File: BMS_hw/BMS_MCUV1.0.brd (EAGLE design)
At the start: 60 x 30 mm, 48 parts, among them IC2 SST25VF020B804ISA, J1 22-27-2051-05, J2 22-27-2051-05, J3 22-27-2041-04, J4 22-27-2051-05, Q2 32.768kHz, U1 NCP1117LP-PG, X1 87758-2016

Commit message: baord sdsahdj
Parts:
- moved R7 50.7 mm to (52.2, 24.6), turned to 270 degrees
- moved U1 49.0 mm to (6.99, 19.1), turned to 90 degrees
- moved C4 38.8 mm to (13.2, 21.6), turned to 270 degrees
- moved IC2 38.2 mm to (42.5, 5.08)
- moved C12 36.7 mm to (57.1, 9.53), turned to 270 degrees
- moved R11 35.1 mm to (10.2, 5.08), turned to 180 degrees
- moved R6 35.1 mm to (49.5, 9.53)
- moved C11 34.8 mm to (47.0, 27.9)
- moved C9 33.6 mm to (49.7, 23.4), turned to 90 degrees
- moved C3 33.3 mm to (17.3, 20.2), turned to 180 degrees
- moved R3 33.0 mm to (43.2, 27.3)
- moved C8 32.5 mm to (50.2, 27.3), turned to 270 degrees
- moved X1 31.1 mm to (27.9, 3.17)
- moved C1 27.4 mm to (38.1, 11.4), turned to 270 degrees
- moved R13 27.3 mm to (14.0, 10.8), turned to 180 degrees
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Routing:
- net CANL: track 137.2 -> 54.3 mm, vias 3 -> 0
- net CANH: track 133.5 -> 58.0 mm, vias 1 -> 2
- net VDD: track 146.3 -> 99.0 mm, vias 6 -> 2
- net CAN_TX: track 10.9 -> 54.3 mm, vias 0 -> 2
- net N$11: track 46.7 -> 7.72 mm, vias 2 -> 0
- net N$19: track 42.9 -> 7.58 mm, vias 2 -> 0
- net DBG_RX: track 29.6 -> 64.5 mm, vias 1 -> 0
- net SCL: track 37.9 -> 3.25 mm, vias 2 -> 0
- net N$6: track 41.2 -> 11.2 mm, vias 2 -> 0
- net N$1: track 42.1 -> 12.3 mm
- net N$8: track 31.0 -> 2.51 mm, vias 2 -> 0
- net N$21: track 32.9 -> 5.03 mm, vias 2 -> 0
- net 3.3V: track 68.6 -> 41.6 mm, vias 3 -> 0
- net N$32: track 64.4 -> 41.4 mm, vias 3 -> 2
- net N$2: track 15.8 -> 38.8 mm, vias 2 -> 0
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
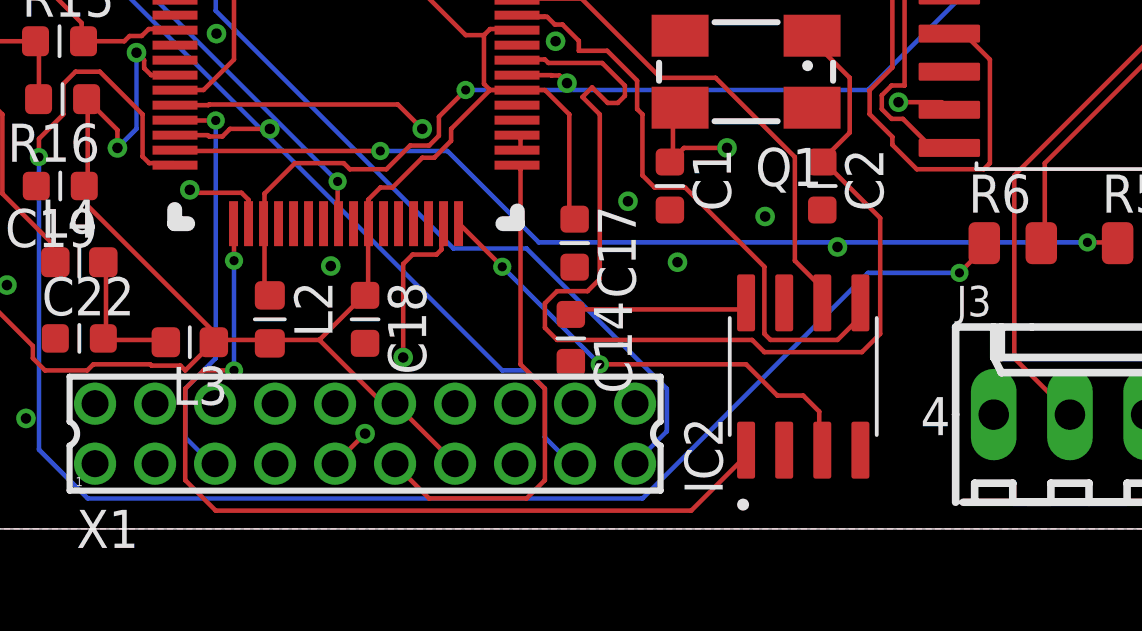
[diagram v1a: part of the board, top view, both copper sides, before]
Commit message: no drc on mcu board
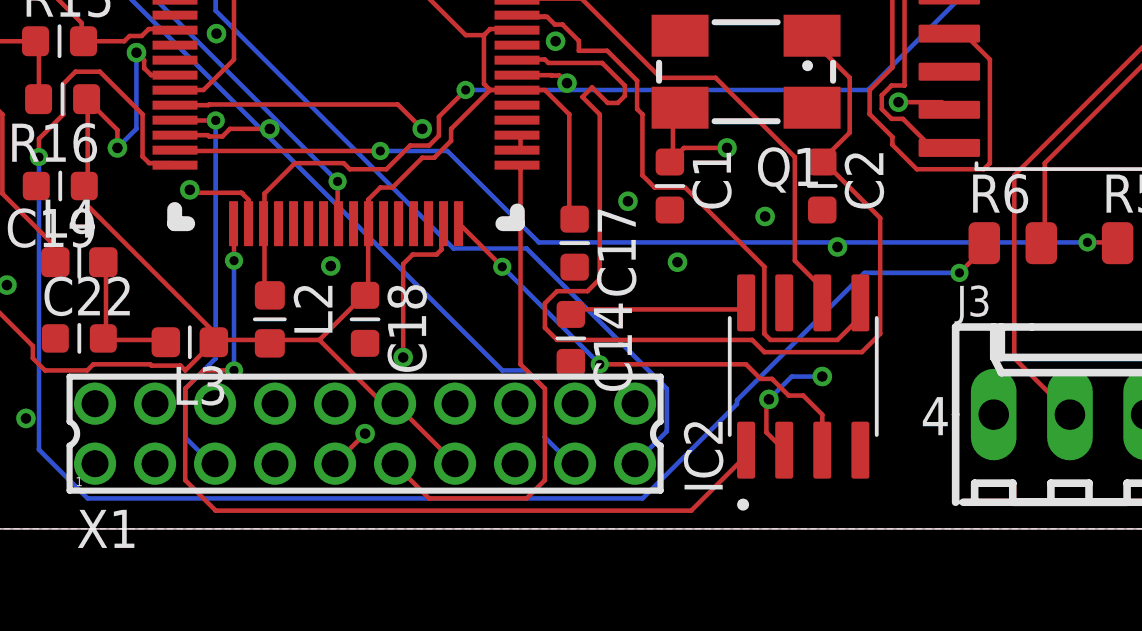
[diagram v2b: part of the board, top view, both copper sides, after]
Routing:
- net SO: track 27.1 -> 31.0 mm, vias 1 -> 3
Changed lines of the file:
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@@
 <contactref element="IC2" pad="2"/>
 <contactref element="MCU2" pad="18"/>
-<wire x1="23.82073125" y1="11.2044" x2="22.225" y2="11.2044" width="0.1524" layer="1"/>
-<wire x1="22.225" y1="11.2044" x2="22.1966" y2="11.2044" width="0.1524" layer="1"/>
-<wire x1="24.055" y1="10.97013125" x2="23.82073125" y2="11.2044" width="0.1524" layer="1"/>
+<wire x1="24.055" y1="10.97013125" x2="23.862565625" y2="11.162565625" width="0.1524" layer="1"/>
+<wire x1="23.862565625" y1="11.162565625" x2="23.82073125" y2="11.2044" width="0.1524" layer="1"/>
 <wire x1="24.055" y1="10.175" x2="24.055" y2="10.97013125" width="0.1524" layer="1"/>
-<wire x1="36.83" y1="11.43" x2="43.18" y2="5.08" width="0.1524" layer="15"/>
+<wire x1="43.18" y1="5.08" x2="36.83" y2="11.43" width="0.1524" layer="15"/>
 <wire x1="26.80465625" y1="11.049" x2="27.24654375" y2="11.049" width="0.1524" layer="15"/>
 <wire x1="22.098" y1="11.303" x2="26.55065625" y2="11.303" width="0.1524" layer="15"/>
-<wire x1="27.62754375" y1="11.43" x2="36.83" y2="11.43" width="0.1524" layer="15"/>
+<wire x1="36.83" y1="11.43" x2="27.62754375" y2="11.43" width="0.1524" layer="15"/>
 <wire x1="26.55065625" y1="11.303" x2="26.80465625" y2="11.049" width="0.1524" layer="15"/>
 <wire x1="27.24654375" y1="11.049" x2="27.62754375" y2="11.43" width="0.1524" layer="15"/>
-<wire x1="43.307" y1="4.953" x2="43.18" y2="5.08" width="0.1524" layer="15"/>
-<wire x1="22.225" y1="11.2044" x2="22.1966" y2="11.2044" width="0.1524" layer="1"/>
+<wire x1="23.862565625" y1="11.162565625" x2="23.82073125" y2="11.2044" width="0.1524" layer="1"/>
 <wire x1="22.1966" y1="11.2044" x2="22.098" y2="11.303" width="0.1524" layer="1"/>
-<via x="22.098" y="11.303" extent="1-15" drill="0.35"/>
-<wire x1="43.307" y1="4.953" x2="41.91" y2="2.625" width="0" layer="19" extent="1-15"/>
+<wire x1="23.82073125" y1="11.2044" x2="22.1966" y2="11.2044" width="0.1524" layer="1"/>
+<via x="22.098" y="11.303" extent="1-16" drill="0.35"/>
+<wire x1="41.3175" y1="3.2175" x2="41.3175" y2="3.2175" width="0.1524" layer="1"/>
+<wire x1="41.3175" y1="3.2175" x2="41.3175" y2="4.2335" width="0.1524" layer="1"/>
+<via x="41.402" y="4.318" extent="1-16" drill="0.35"/>
+<wire x1="41.402" y1="4.318" x2="42.164" y2="5.08" width="0.1524" layer="16"/>
+<via x="43.18" y="5.08" extent="15-16" drill="0.35"/>
+<wire x1="42.164" y1="5.08" x2="43.18" y2="5.08" width="0.1524" layer="16"/>
+<wire x1="41.3175" y1="3.2175" x2="41.91" y2="2.625" width="0.1524" layer="1"/>
+<wire x1="41.3175" y1="4.2335" x2="41.402" y2="4.318" width="0.1524" layer="1"/>
 </signal>
 <signal name="WP#">
@@
 <wire x1="35.7632" y1="5.4864" x2="40.64" y2="5.4864" width="0.1524" layer="1"/>
 <wire x1="31.0896" y1="10.16" x2="31.055" y2="10.175" width="0.1524" layer="1"/>
-<wire x1="43.0784" y1="2.6416" x2="43.092475" y2="2.6393" width="0.1524" layer="1"/>
 <via x="32.512" y="8.7376" extent="1-16" drill="0.3048"/>
 <via x="35.7632" y="5.4864" extent="1-16" drill="0.3048"/>
-<wire x1="43.092475" y1="2.6393" x2="43.18" y2="2.625" width="0.1524" layer="1"/>
-<wire x1="40.64" y1="5.4864" x2="41.6814" y2="4.445" width="0.1524" layer="1"/>
-<wire x1="41.6814" y1="4.445" x2="42.545" y2="4.445" width="0.1524" layer="1"/>
-<wire x1="42.545" y1="4.445" x2="43.0784" y2="3.9116" width="0.1524" layer="1"/>
-<wire x1="43.0784" y1="3.9116" x2="43.0784" y2="2.653375" width="0.1524" layer="1"/>
-<wire x1="43.0784" y1="2.653375" x2="43.092475" y2="2.6393" width="0.1524" layer="1"/>
+<wire x1="43.18" y1="3.81" x2="43.18" y2="2.625" width="0.1524" layer="1"/>
+<wire x1="42.545" y1="4.445" x2="43.18" y2="3.81" width="0.1524" layer="1"/>
+<wire x1="40.64" y1="5.4864" x2="41.1254" y2="5.001" width="0.1524" layer="1"/>
+<wire x1="41.1254" y1="5.001" x2="41.50530625" y2="5.001" width="0.1524" layer="1"/>
+<wire x1="42.06130625" y1="4.445" x2="42.545" y2="4.445" width="0.1524" layer="1"/>
+<wire x1="41.50530625" y1="5.001" x2="42.06130625" y2="4.445" width="0.1524" layer="1"/>
 </signal>
 <signal name="SI">
@@
 <contactref element="MCU2" pad="16"/>
 <wire x1="47.752" y1="8.5344" x2="48.5648" y2="9.3472" width="0.1524" layer="1"/>
-<wire x1="44.704" y1="8.5344" x2="47.752" y2="8.5344" width="0.1524" layer="16"/>
-<wire x1="37.1856" y1="1.016" x2="44.704" y2="8.5344" width="0.1524" layer="16"/>
 <wire x1="18.6944" y1="1.016" x2="37.1856" y2="1.016" width="0.1524" layer="16"/>
 <wire x1="17.0688" y1="2.6416" x2="18.6944" y2="1.016" width="0.1524" layer="16"/>
@@
 <wire x1="20.74286875" y1="12.192" x2="20.5232" y2="12.41166875" width="0.1524" layer="1"/>
 <wire x1="20.5232" y1="12.41166875" x2="20.5232" y2="13.8176" width="0.1524" layer="1"/>
+<wire x1="37.1856" y1="1.016" x2="40.338" y2="4.1684" width="0.1524" layer="16"/>
+<wire x1="40.338" y1="4.1684" x2="40.338" y2="4.28510625" width="0.1524" layer="16"/>
+<wire x1="40.338" y1="4.28510625" x2="44.58729375" y2="8.5344" width="0.1524" layer="16"/>
+<wire x1="44.58729375" y1="8.5344" x2="47.752" y2="8.5344" width="0.1524" layer="16"/>
 </signal>
 <signal name="!MCLR">

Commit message: defsdf
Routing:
- net 3.3V: track 41.6 -> 45.7 mm, vias 0 -> 2
- added copper zone on layer 1, net 3.3V
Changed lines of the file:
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@@
 <via x="19.812" y="18.796" extent="1-2" drill="0.35"/>
 <via x="22.987" y="16.51" extent="1-2" drill="0.35"/>
-<via x="13.081" y="18.923" extent="1-2" drill="0.35"/>
+<via x="14.732" y="19.304" extent="1-2" drill="0.35"/>
 <via x="16.637" y="3.683" extent="1-2" drill="0.35"/>
 <via x="16.002" y="8.128" extent="1-2" drill="0.35"/>
@@
 <wire x1="9.9568" y1="19.1008" x2="8.7376" y2="20.32" width="0.1524" layer="1"/>
 <wire x1="16.256" y1="25.4" x2="16.51" y2="25.665" width="0.1524" layer="1"/>
-<wire x1="9.9568" y1="19.1008" x2="10.135" y2="19.05" width="0.1524" layer="1"/>
+<wire x1="10.135" y1="19.05" x2="9.9568" y2="19.1008" width="0.1524" layer="1"/>
+<polygon width="0.1524" layer="1">
+<vertex x="8.89" y="20.32"/>
+<vertex x="12.065" y="20.32"/>
+<vertex x="13.97" y="18.415"/>
+<vertex x="9.525" y="18.415"/>
+<vertex x="9.525" y="19.685"/>
+</polygon>
+<polygon width="0.1524" layer="1">
+<vertex x="17.78" y="25.4"/>
+<vertex x="17.78" y="23.495"/>
+<vertex x="18.415" y="23.495"/>
+<vertex x="19.05" y="24.13"/>
+<vertex x="19.685" y="24.13"/>
+<vertex x="20.32" y="24.765"/>
+<vertex x="20.32" y="25.4"/>
+</polygon>
+<wire x1="10.135" y1="19.05" x2="11.43" y2="19.05" width="0.1524" layer="1"/>
+<via x="12.192" y="19.812" extent="1-16" drill="0.3048"/>
+<wire x1="11.43" y1="19.05" x2="12.192" y2="19.812" width="0.1524" layer="1"/>
+<wire x1="12.192" y1="19.812" x2="12.7" y2="19.304" width="0.1524" layer="16"/>
+<wire x1="12.7" y1="19.304" x2="12.7" y2="19.05" width="0.1524" layer="16"/>
+<wire x1="12.7" y1="19.05" x2="12.319" y2="19.05" width="0.1524" layer="16"/>
+<wire x1="12.319" y1="19.05" x2="12.065" y2="18.796" width="0.1524" layer="16"/>
+<via x="12.065" y="18.796" extent="15-16" drill="0.3048"/>
 </signal>
 <signal name="N$6">
@@
 <wire x1="14.8336" y1="10.9728" x2="14.0208" y2="11.7856" width="0.1524" layer="1"/>
 <wire x1="11.176" y1="8.3312" x2="11.11" y2="8.255" width="0.1524" layer="1"/>
-<wire x1="14.8336" y1="10.9728" x2="14.92" y2="10.795" width="0.1524" layer="1"/>
+<wire x1="14.92" y1="10.795" x2="14.8336" y2="10.9728" width="0.1524" layer="1"/>
 <wire x1="10.16" y1="24.1808" x2="10.16" y2="26.67" width="0.1524" layer="1"/>
 <wire x1="8.3312" y1="22.352" x2="10.16" y2="24.1808" width="0.1524" layer="1"/>
@@
 <contactref element="X1" pad="19"/>
 <contactref element="MCU2" pad="1"/>
-<wire x1="22.352" y1="19.7104" x2="21.7424" y2="19.7104" width="0.1524" layer="1"/>
-<wire x1="22.9616" y1="19.1008" x2="22.352" y2="19.7104" width="0.1524" layer="1"/>
 <wire x1="22.9616" y1="17.272" x2="22.9616" y2="19.1008" width="0.1524" layer="16"/>
 <wire x1="30.8864" y1="9.3472" x2="22.9616" y2="17.272" width="0.1524" layer="16"/>
@@
 <wire x1="37.9984" y1="3.2512" x2="37.9984" y2="4.6736" width="0.1524" layer="16"/>
 <wire x1="36.9824" y1="2.2352" x2="37.9984" y2="3.2512" width="0.1524" layer="16"/>
-<wire x1="21.7424" y1="19.7104" x2="21.605" y2="19.625" width="0.1524" layer="1"/>
 <wire x1="36.94" y1="2.175" x2="36.9824" y2="2.2352" width="0.1524" layer="16"/>
 <via x="22.9616" y="19.1008" extent="1-16" drill="0.3048"/>
+<wire x1="21.605" y1="19.625" x2="22.4374" y2="19.625" width="0.1524" layer="1"/>
+<wire x1="22.4374" y1="19.625" x2="22.9616" y2="19.1008" width="0.1524" layer="1"/>
 </signal>
 <signal name="INTL_OUT">

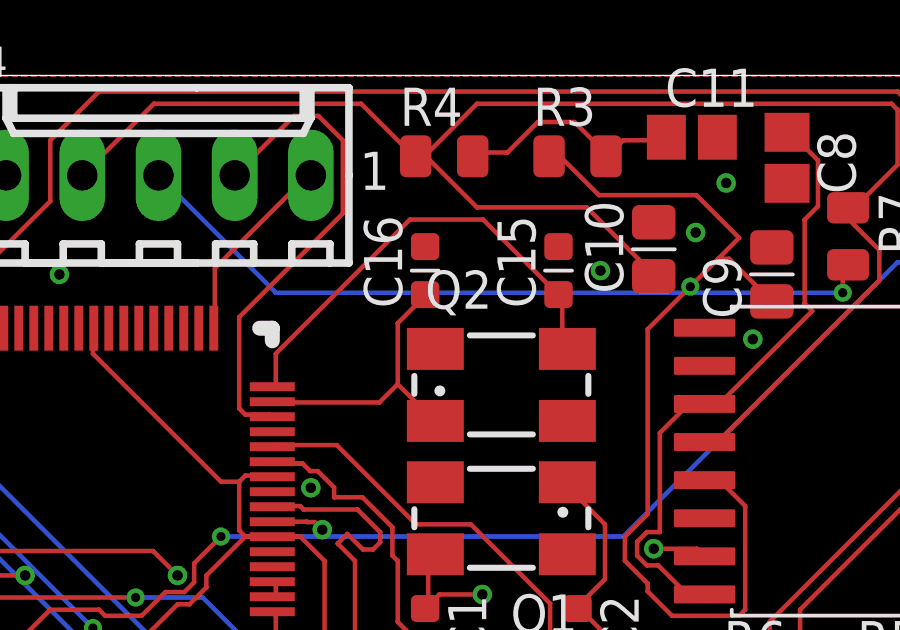
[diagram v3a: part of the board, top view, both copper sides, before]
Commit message: secondary osc removed
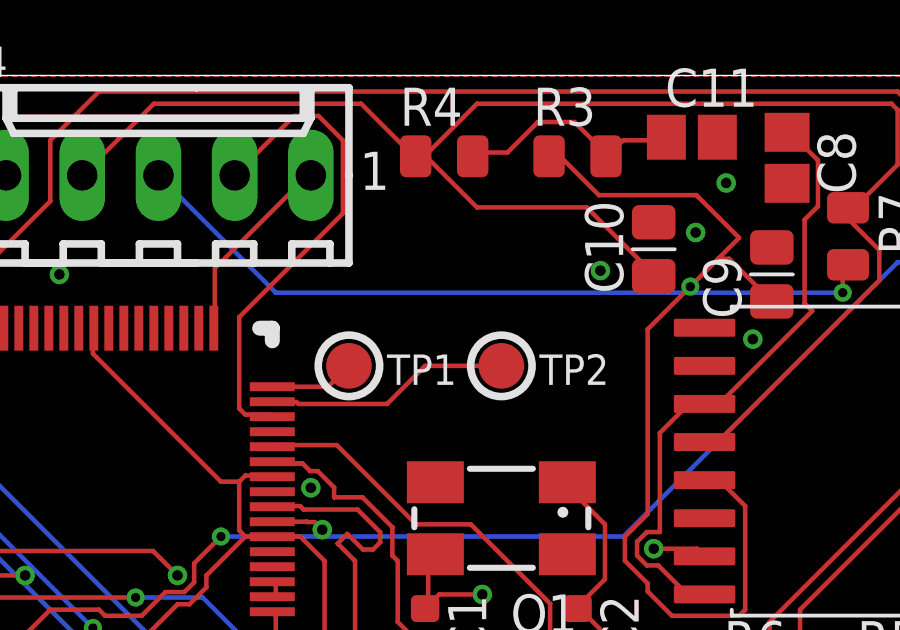
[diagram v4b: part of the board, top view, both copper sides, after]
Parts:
- removed C15, C16: 11pF, ipc-7351-capacitor:CAPC1608X92N
- removed Q2: 32.768kHz, adafruit:CTS406
- added TP1, TP2: TP-SMD60, simpa:TP-SMD60
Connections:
- removed net N$17: C16.1, MCU2.47, Q2.1
- new net N$5: MCU2.48, TP1.P$1
- net GND: no longer C15.2, C16.2
- net N$16: now also MCU2.47, TP2.P$1; no longer C15.1, MCU2.48, Q2.3
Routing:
- net N$17: track 9.55 -> 0.00 mm
- net N$16: track 15.5 -> 8.19 mm
- net N$5: track 0.00 -> 2.84 mm
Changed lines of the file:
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@@
 <element name="C13" library="ipc-7351-capacitor" package="CAPC2012X145AN" value="" x="20.701" y="26.289" rot="R90"/>
 <element name="C14" library="ipc-7351-capacitor" package="CAPC1608X92N" value="0.1uF" x="34.798" y="6.35" rot="R270"/>
-<element name="C15" library="ipc-7351-capacitor" package="CAPC1608X92N" value="11pF" x="42.545" y="23.495" rot="R90"/>
-<element name="C16" library="ipc-7351-capacitor" package="CAPC1608X92N" value="11pF" x="38.1" y="23.495" rot="R90"/>
 <element name="C17" library="ipc-7351-capacitor" package="CAPC1608X92N" value=".1uF" x="34.925" y="9.525" rot="R270"/>
 <element name="C18" library="ipc-7351-capacitor" package="CAPC1608X92N" value=".1uF" x="27.94" y="6.985" rot="R270"/>
@@
 <attribute name="OC_NEWARK" value="unknown" x="40.64" y="15.24" size="1.778" layer="27" rot="R180" display="off"/>
 </element>
-<element name="Q2" library="adafruit" package="CTS406" value="32.768kHz" x="40.64" y="19.685">
-<attribute name="MF" value="" x="40.64" y="19.685" size="1.778" layer="27" display="off"/>
-<attribute name="MPN" value="" x="40.64" y="19.685" size="1.778" layer="27" display="off"/>
-<attribute name="OC_FARNELL" value="unknown" x="40.64" y="19.685" size="1.778" layer="27" display="off"/>
-<attribute name="OC_NEWARK" value="unknown" x="40.64" y="19.685" size="1.778" layer="27" display="off"/>
-</element>
 <element name="R10" library="ipc-7351-resistor" package="RESC2012X70N" value="10" x="10.16" y="8.255" rot="R180"/>
 <element name="R11" library="ipc-7351-resistor" package="RESC2012X70N" value="100" x="10.16" y="5.08" rot="R180"/>
@@
 <element name="C3" library="ipc-7351-capacitor" package="CAPC1608X92N" value=".01uF" x="17.272" y="20.193" rot="R180"/>
 <element name="C4" library="ipc-7351-capacitor" package="CAPC1608X92N" value=".01uF" x="13.208" y="21.59" rot="R270"/>
+<element name="TP1" library="simpa" package="TP-SMD60" value="TP-SMD60" x="35.56" y="20.32"/>
+<element name="TP2" library="simpa" package="TP-SMD60" value="TP-SMD60" x="40.64" y="20.32"/>
 </elements>
 <signals>
@@
 <contactref element="C14" pad="2"/>
 <contactref element="IC2" pad="4"/>
-<contactref element="C15" pad="2"/>
-<contactref element="C16" pad="2"/>
 <contactref element="X1" pad="2"/>
 <contactref element="X1" pad="7"/>
@@
 <wire x1="33.1216" y1="17.6784" x2="33.005" y2="17.625" width="0.1524" layer="1"/>
 <wire x1="43.18" y1="7.535" x2="43.0784" y2="7.7216" width="0.1524" layer="1"/>
-</signal>
-<signal name="N$16">
-<contactref element="C15" pad="1"/>
-<contactref element="Q2" pad="3"/>
-<contactref element="MCU2" pad="48"/>
-<wire x1="42.672" y1="20.9296" x2="42.672" y2="22.5552" width="0.1524" layer="1"/>
-<wire x1="42.672" y1="22.5552" x2="42.545" y2="22.695" width="0.1524" layer="1"/>
-<wire x1="42.672" y1="20.9296" x2="42.84" y2="20.885" width="0.1524" layer="1"/>
-<wire x1="33.1216" y1="20.7264" x2="33.1216" y2="19.7104" width="0.1524" layer="1"/>
-<wire x1="37.592" y1="25.1968" x2="33.1216" y2="20.7264" width="0.1524" layer="1"/>
-<wire x1="40.0304" y1="25.1968" x2="37.592" y2="25.1968" width="0.1524" layer="1"/>
-<wire x1="42.4688" y1="22.7584" x2="40.0304" y2="25.1968" width="0.1524" layer="1"/>
-<wire x1="33.1216" y1="19.7104" x2="33.005" y2="19.625" width="0.1524" layer="1"/>
-<wire x1="42.4688" y1="22.7584" x2="42.545" y2="22.695" width="0.1524" layer="1"/>
 </signal>
 <signal name="VDD">
@@
 <wire x1="33.1216" y1="13.0048" x2="33.005" y2="13.125" width="0.1524" layer="1"/>
 </signal>
-<signal name="N$17">
-<contactref element="Q2" pad="1"/>
+<signal name="N$5">
+<contactref element="TP1" pad="P$1"/>
+<contactref element="MCU2" pad="48"/>
+<wire x1="33.005" y1="19.625" x2="34.865" y2="19.625" width="0.1524" layer="1"/>
+<wire x1="34.865" y1="19.625" x2="35.56" y2="20.32" width="0.1524" layer="1"/>
+</signal>
+<signal name="N$16">
+<contactref element="TP2" pad="P$1"/>
 <contactref element="MCU2" pad="47"/>
-<contactref element="C16" pad="1"/>
-<wire x1="37.1856" y1="21.7424" x2="37.9984" y2="22.5552" width="0.1524" layer="1"/>
-<wire x1="37.1856" y1="19.7104" x2="37.1856" y2="21.7424" width="0.1524" layer="1"/>
-<wire x1="38.4048" y1="18.4912" x2="37.1856" y2="19.7104" width="0.1524" layer="1"/>
-<wire x1="37.9984" y1="22.5552" x2="38.1" y2="22.695" width="0.1524" layer="1"/>
-<wire x1="38.4048" y1="18.4912" x2="38.44" y2="18.485" width="0.1524" layer="1"/>
-<wire x1="36.576" y1="19.1008" x2="33.1216" y2="19.1008" width="0.1524" layer="1"/>
-<wire x1="37.1856" y1="19.7104" x2="36.576" y2="19.1008" width="0.1524" layer="1"/>
-<wire x1="33.1216" y1="19.1008" x2="33.005" y2="19.125" width="0.1524" layer="1"/>
+<wire x1="40.64" y1="20.32" x2="38.1" y2="20.32" width="0.1524" layer="1"/>
+<wire x1="38.1" y1="20.32" x2="36.83" y2="19.05" width="0.1524" layer="1"/>
+<wire x1="36.83" y1="19.05" x2="33.87513125" y2="19.05" width="0.1524" layer="1"/>
+<wire x1="33.015978125" y1="19.114021875" x2="33.005" y2="19.125" width="0.1524" layer="1"/>
+<wire x1="33.87513125" y1="19.05" x2="33.811109375" y2="19.114021875" width="0.1524" layer="1"/>
+<wire x1="33.811109375" y1="19.114021875" x2="33.015978125" y2="19.114021875" width="0.1524" layer="1"/>
 </signal>
 </signals>

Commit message: placment 80% done
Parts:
- added X2, X3: (no value), con-molex:KK-156-10
- moved IC2 120.3 mm to (141.0, -64.1)
- moved U$1 106.8 mm to (97.8, -79.4)
- moved C11 104.2 mm to (79.4, -71.1)
- moved R3 101.9 mm to (79.4, -67.9)
- moved R6 99.6 mm to (80.6, -85.1)
- moved C10 94.9 mm to (78.7, -64.8), turned to 180 degrees
- moved R5 94.6 mm to (80.6, -81.3)
- moved C4 92.8 mm to (13.3, -71.2), turned to 0 degrees
- moved R12 90.8 mm to (14.0, -87.6)
- moved C8 89.1 mm to (78.8, -57.1), turned to 0 degrees
- moved C9 89.1 mm to (78.9, -60.8), turned to 180 degrees
- moved R11 89.0 mm to (13.3, -83.8)
- moved C12 88.7 mm to (80.0, -76.2), turned to 0 degrees
- moved R14 87.0 mm to (13.4, -80.6)
- moved J1 86.7 mm to (-8.26, -77.5)
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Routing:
- net VDD: track 99.0 -> 0.00 mm, vias 2 -> 0
- net DBG_RX: track 64.5 -> 0.00 mm
- net CANH: track 58.0 -> 0.00 mm, vias 2 -> 0
- net CAN_TX: track 54.4 -> 0.00 mm, vias 2 -> 0
- net CANL: track 54.3 -> 0.00 mm
- net 3.3V: track 45.7 -> 0.00 mm, vias 2 -> 0
- net N$32: track 41.4 -> 0.00 mm, vias 2 -> 0
- net DBG_TX: track 39.1 -> 0.00 mm, vias 1 -> 0
- net N$2: track 38.8 -> 0.00 mm
- net 15V_AUX: track 33.8 -> 0.00 mm, vias 1 -> 0
- net ICSPDAT: track 33.6 -> 0.00 mm
- net CAN_RX: track 32.7 -> 0.00 mm, vias 2 -> 0
- net ICSPCLK: track 32.1 -> 0.00 mm, vias 1 -> 0
- net SO: track 31.0 -> 0.00 mm, vias 3 -> 0
- net CE#: track 29.9 -> 0.00 mm, vias 2 -> 0
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- removed copper zone on layer 1, net 3.3V
